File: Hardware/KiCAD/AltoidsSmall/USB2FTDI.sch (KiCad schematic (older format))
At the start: 13 parts, among them U3 FT230XQ

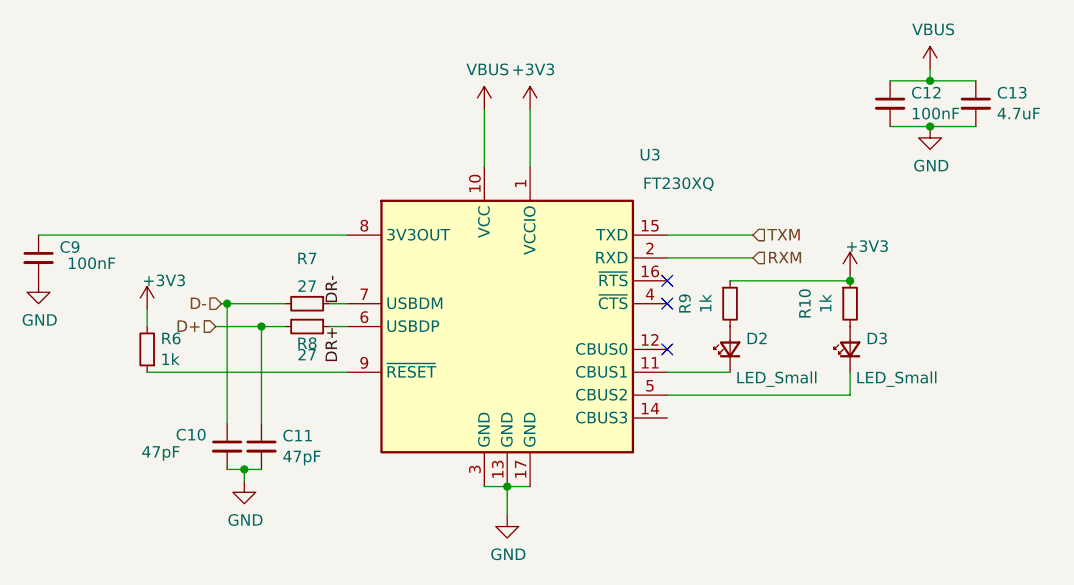
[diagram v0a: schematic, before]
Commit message: Added labels to pins, Added part numbers
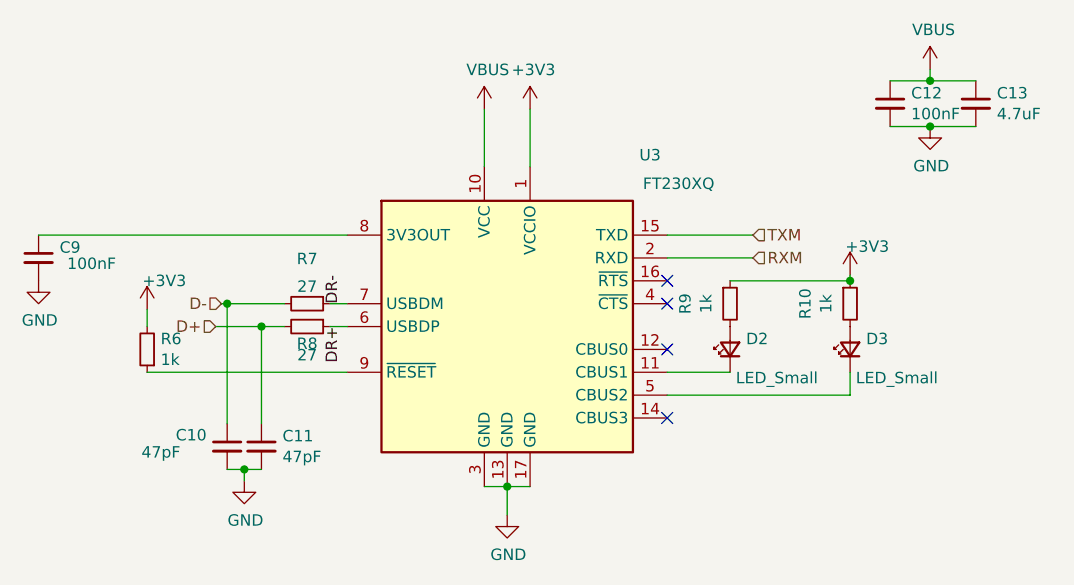
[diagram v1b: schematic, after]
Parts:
- C10, C11: Digikey (none) -> 311-4037-1-ND
- C12, C9: Digikey (none) -> 1276-CL10B104KB8VPJCCT-ND
- D2, D3: footprint Capacitor_SMD:C_0603_1608Metric_Pad1.05x0.95mm_HandSolder -> Diode_SMD:D_0603_1608Metric_Castellated; Digikey (none) -> 475-1276-1-ND
- R7, R8: Digikey (none) -> RR08Q27DCT-ND
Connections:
- no-connect marks 3 -> 4
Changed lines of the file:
@@
 F 0 "D3" V 7046 3630 50  0000 R CNN
 F 1 "LED_Small" V 6875 3675 50  0000 R CNN
-F 2 "Capacitor_SMD:C_0603_1608Metric_Pad1.05x0.95mm_HandSolder" V 7000 3700 50  0001 C CNN
+F 2 "Diode_SMD:D_0603_1608Metric_Castellated" V 7000 3700 50  0001 C CNN
 F 3 "~" V 7000 3700 50  0001 C CNN
+F 4 "475-1276-1-ND" V 7000 3700 50  0001 C CNN "Digikey"
 	1    7000 3700
 	0    -1   -1   0
@@
 F 2 "Resistor_SMD:R_0603_1608Metric_Pad1.05x0.95mm_HandSolder" H 4625 3500 50  0001 C CNN
 F 3 "~" H 4625 3500 50  0001 C CNN
+F 4 "RR08Q27DCT-ND" V 4625 3500 50  0001 C CNN "Digikey"
 	1    4625 3500
 	0    1    1    0
@@
 F 2 "Resistor_SMD:R_0603_1608Metric_Pad1.05x0.95mm_HandSolder" H 4625 3600 50  0001 C CNN
 F 3 "~" H 4625 3600 50  0001 C CNN
+F 4 "RR08Q27DCT-ND" V 4625 3600 50  0001 C CNN "Digikey"
 	1    4625 3600
 	0    1    1    0
@@
 F 2 "Capacitor_SMD:C_0603_1608Metric_Pad1.05x0.95mm_HandSolder" H 4275 4125 50  0001 C CNN
 F 3 "~" H 4275 4125 50  0001 C CNN
+F 4 "311-4037-1-ND" H 4275 4125 50  0001 C CNN "Digikey"
 	1    4275 4125
 	1    0    0    -1
@@
 F 2 "Capacitor_SMD:C_0603_1608Metric_Pad1.05x0.95mm_HandSolder" H 4425 4125 50  0001 C CNN
 F 3 "~" H 4425 4125 50  0001 C CNN
+F 4 "311-4037-1-ND" H 4425 4125 50  0001 C CNN "Digikey"
 	1    4425 4125
 	1    0    0    -1
@@
 F 2 "Capacitor_SMD:C_0603_1608Metric_Pad1.05x0.95mm_HandSolder" H 7175 2625 50  0001 C CNN
 F 3 "~" H 7175 2625 50  0001 C CNN
+F 4 "1276-CL10B104KB8VPJCCT-ND" H 7175 2625 50  0001 C CNN "Digikey"
 	1    7175 2625
 	1    0    0    -1
@@
 F 2 "Capacitor_SMD:C_0603_1608Metric_Pad1.05x0.95mm_HandSolder" H 3450 3300 50  0001 C CNN
 F 3 "~" H 3450 3300 50  0001 C CNN
+F 4 "1276-CL10B104KB8VPJCCT-ND" H 3450 3300 50  0001 C CNN "Digikey"
 	1    3450 3300
 	1    0    0    -1
@@
 F 0 "D2" V 6521 3630 50  0000 R CNN
 F 1 "LED_Small" V 6350 3675 50  0000 R CNN
-F 2 "Capacitor_SMD:C_0603_1608Metric_Pad1.05x0.95mm_HandSolder" V 6475 3700 50  0001 C CNN
+F 2 "Diode_SMD:D_0603_1608Metric_Castellated" V 6475 3700 50  0001 C CNN
 F 3 "~" V 6475 3700 50  0001 C CNN
+F 4 "475-1276-1-ND" V 6475 3700 50  0001 C CNN "Digikey"
 	1    6475 3700
 	0    -1   -1   0
@@
 Wire Wire Line
 	7000 3800 7000 3900
+NoConn ~ 6200 4000
 $EndSCHEMATC
